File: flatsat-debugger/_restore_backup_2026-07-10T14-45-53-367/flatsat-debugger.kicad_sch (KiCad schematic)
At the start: 0 parts

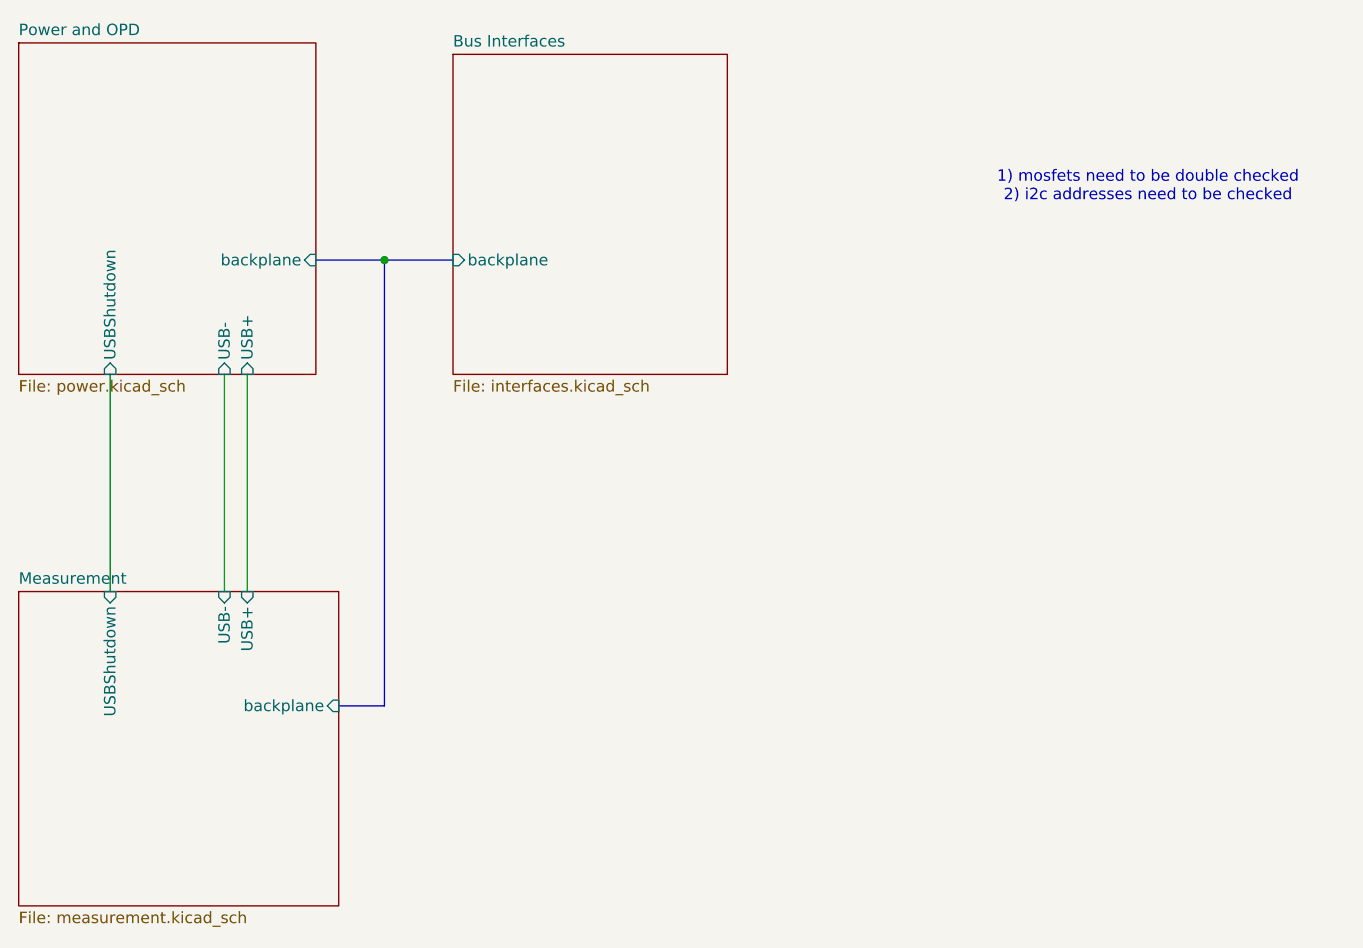
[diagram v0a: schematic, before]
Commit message: hierarchical sheets and fixes
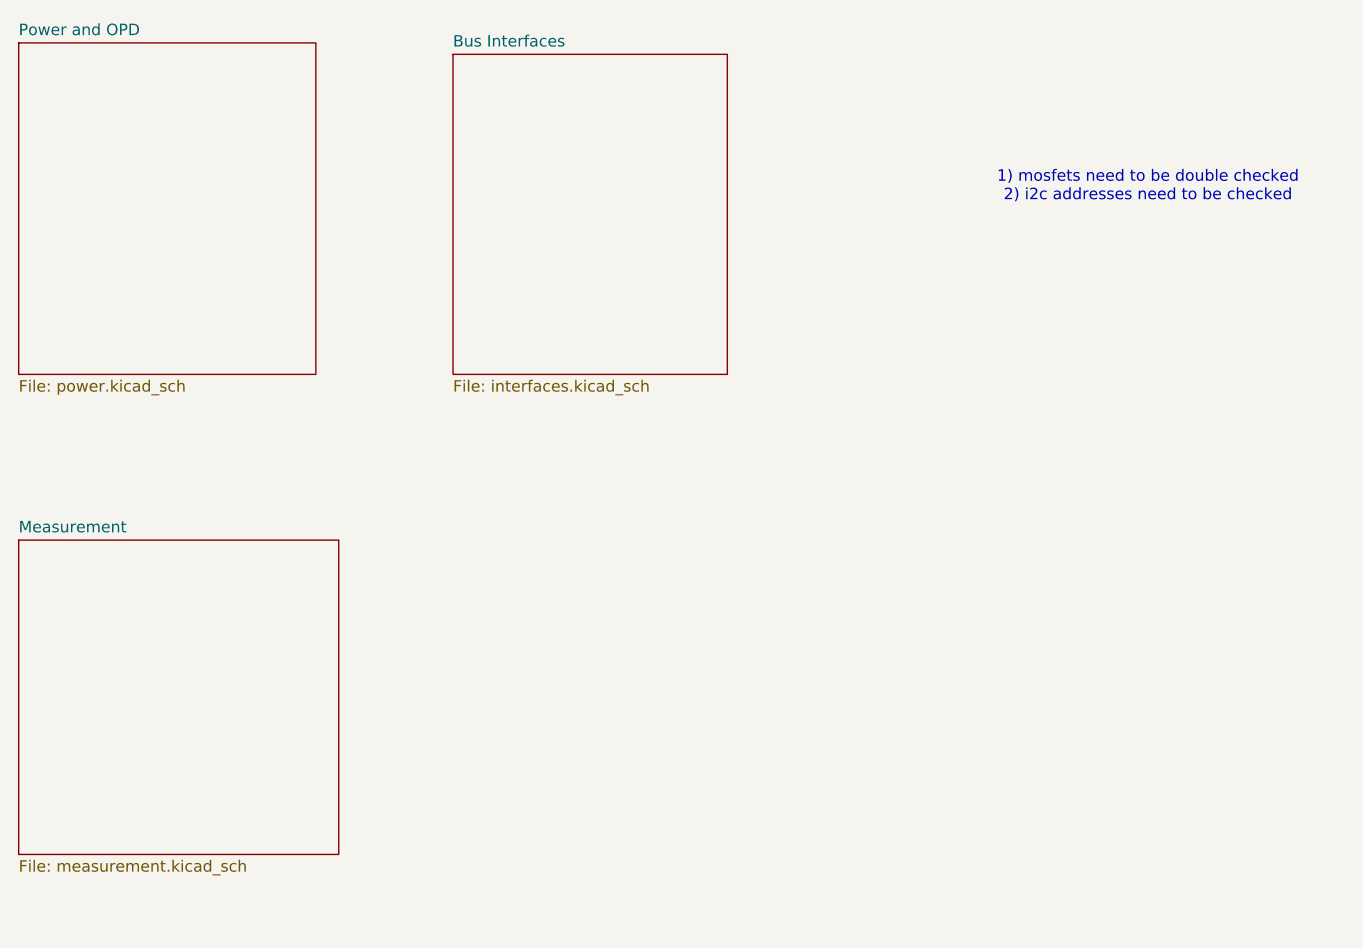
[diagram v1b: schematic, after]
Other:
- sheet Bus Interfaces ports: added none; removed backplane
- sheet Measurement ports: added none; removed USB+, USB-, USBShutdown, backplane
- sheet Power and OPD ports: added none; removed USB+, USB-, USBShutdown, backplane
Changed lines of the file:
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@@
 		)
 	)
-	(junction
-		(at 137.16 62.23)
-		(diameter 0)
-		(color 0 0 0 0)
-	)
-	(bus
-		(pts
-			(xy 129.54 62.23) (xy 137.16 62.23)
-		)
-		(stroke
-			(width 0)
-			(type default)
-		)
-	)
-	(bus
-		(pts
-			(xy 132.08 111.76) (xy 137.16 111.76)
-		)
-		(stroke
-			(width 0)
-			(type default)
-		)
-	)
-	(bus
-		(pts
-			(xy 137.16 62.23) (xy 144.78 62.23)
-		)
-		(stroke
-			(width 0)
-			(type default)
-		)
-	)
-	(wire
-		(pts
-			(xy 121.92 74.93) (xy 121.92 99.06)
-		)
-		(stroke
-			(width 0)
-			(type default)
-		)
-	)
-	(wire
-		(pts
-			(xy 119.38 74.93) (xy 119.38 99.06)
-		)
-		(stroke
-			(width 0)
-			(type default)
-		)
-	)
-	(bus
-		(pts
-			(xy 137.16 62.23) (xy 137.16 111.76)
-		)
-		(stroke
-			(width 0)
-			(type default)
-		)
-	)
-	(wire
-		(pts
-			(xy 106.68 74.93) (xy 106.68 99.06)
-		)
-		(stroke
-			(width 0)
-			(type default)
-		)
-	)
 	(image
 		(at 257.81 173.99)
@@
 			)
 		)
-		(pin "backplane" input
-			(at 144.78 62.23 180)
-			(effects
-				(font
-					(size 1.27 1.27)
-				)
-				(justify left)
-			)
-		)
 		(instances
-			(project "flatsat-interface-card"
+			(project "flatsat-debugger"
 				(path "/1a9202c4-e698-4c93-952c-ee3e64e9e49c"
 					(page "3")
@@
 			)
 		)
-		(pin "USB+" input
-			(at 121.92 74.93 270)
-			(effects
-				(font
-					(size 1.27 1.27)
-				)
-				(justify left)
-			)
-		)
-		(pin "USB-" input
-			(at 119.38 74.93 270)
-			(effects
-				(font
-					(size 1.27 1.27)
-				)
-				(justify left)
-			)
-		)
-		(pin "USBShutdown" input
-			(at 106.68 74.93 270)
-			(effects
-				(font
-					(size 1.27 1.27)
-				)
-				(justify left)
-			)
-		)
-		(pin "backplane" input
-			(at 129.54 62.23 0)
-			(effects
-				(font
-					(size 1.27 1.27)
-				)
-				(justify right)
-			)
-		)
 		(instances
-			(project "flatsat-interface-card"
+			(project "flatsat-debugger"
 				(path "/1a9202c4-e698-4c93-952c-ee3e64e9e49c"
 					(page "2")
@@
 	)
 	(sheet
-		(at 96.52 99.06)
+		(at 96.52 93.345)
 		(size 35.56 34.925)
 		(exclude_from_sim no)
@@
 		)
 		(property "Sheetname" "Measurement"
-			(at 96.52 98.3484 0)
+			(at 96.52 92.6334 0)
 			(show_name no)
 			(do_not_autoplace no)
@@
 		)
 		(property "Sheetfile" "measurement.kicad_sch"
-			(at 96.52 134.5696 0)
+			(at 96.52 128.8546 0)
 			(show_name no)
 			(do_not_autoplace no)
@@
 		)
 		(property "Field2" ""
-			(at 96.52 99.06 0)
+			(at 96.52 93.345 0)
 			(hide yes)
 			(show_name no)
@@
 			)
 		)
-		(pin "backplane" input
-			(at 132.08 111.76 0)
-			(effects
-				(font
-					(size 1.27 1.27)
-				)
-				(justify right)
-			)
-		)
-		(pin "USBShutdown" input
-			(at 106.68 99.06 90)
-			(effects
-				(font
-					(size 1.27 1.27)
-				)
-				(justify right)
-			)
-		)
-		(pin "USB-" input
-			(at 119.38 99.06 90)
-			(effects
-				(font
-					(size 1.27 1.27)
-				)
-				(justify right)
-			)
-		)
-		(pin "USB+" input
-			(at 121.92 99.06 90)
-			(effects
-				(font
-					(size 1.27 1.27)
-				)
-				(justify right)
-			)
-		)
 		(instances
-			(project "flatsat-interface-card"
+			(project "flatsat-debugger"
 				(path "/1a9202c4-e698-4c93-952c-ee3e64e9e49c"
 					(page "4")
